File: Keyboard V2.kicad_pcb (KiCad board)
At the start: 4 copper layers, 317.8 x 142.5 mm, 239 parts, among them J1 Conn_01x05_Pin, J2 USB_C_Receptacle_USB2.0_16P, P1 SW_Push, SW1 ESC, SW10 F9, SW11 F10, SW12 F11, SW13 F12, SW14 PrntScrn, SW15 Til, SW16 1, SW17 2, SW18 3, SW19 4, SW2 F1, SW20 5, SW21 6, SW22 7, SW23 8, SW24 RotaryEncoder_Switch, SW25 9, SW26 0, SW27 Min, SW28 Plus, SW29 Bs, SW3 F2, SW30 Del, SW31 Tab, SW32 Q, SW33 W, SW34 E, SW35 R, SW36 T, SW37 Y, SW38 U, SW39 I, SW4 F3, SW40 O, SW41 P, SW42 LBrck, SW43 RBrck, SW44 BSlsh, SW45 Home, SW46 Caps, SW47 A, SW48 S, SW49 D, SW5 F4, SW50 F, SW51 G, SW52 H, SW53 J, SW54 K, SW55 L, SW56 Semi, SW57 Quot, SW58 Enter, SW59 End, SW6 F5, SW60 LShft, SW61 Z, SW62 X, SW63 C, SW64 V, SW65 B, SW66 N, SW67 M, SW68 Comma, SW69 Prd, SW7 F6, SW70 Slash, SW71 RShft, SW72 Up, SW73 LCtrl, SW74 Supr, SW75 Alt, SW76 Space, SW77 RAlt, SW78 Fn, SW79 Left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

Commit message: finish esp32-31 version
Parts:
- removed C109: 1uF, Capacitor_SMD:C_0402_1005Metric
- removed C111, C96, C97: 2.2uF, Capacitor_SMD:C_0402_1005Metric
- removed C112, C113, C114, C117, C92, C93, C94, C95: 100nF, Capacitor_SMD:C_0402_1005Metric
- removed the C78 at (339.4, 17.9)
- removed C88: 100nF, Capacitor_SMD:C_0603_1608Metric
- removed C89: 10uF, Capacitor_SMD:C_0805_2012Metric
- removed C90: 30pF, Capacitor_SMD:C_0402_1005Metric
- removed FB1: FerriteBead, Inductor_SMD:L_0603_1608Metric
- removed FID1, FID2, FID3: Fiducial, Fiducial:Fiducial_1mm_Mask2mm
- removed the R13 at (322.9, 21.0)
- removed the R16 at (321.8, 21.0)
- removed R19: 1k, Resistor_SMD:R_0603_1608Metric
- removed U2: STM32F723IEK6, STM32F723IEK6:IC_STM32F723IEK6
- removed Y1: Crystal_GND24, Crystal:Crystal_SMD_Abracon_ABM8G-4Pin_3.2x2.5mm
- added C100: 100nF, Capacitor_SMD:C_0402_1005Metric, F.Cu at (343.4, 35.5)
- added C101: 100nF, Capacitor_SMD:C_0402_1005Metric, F.Cu at (342.1, 38.7)
- added C102: 100nF, Capacitor_SMD:C_0402_1005Metric, F.Cu at (342.1, 41.8)
- added C103: 1uF, Capacitor_SMD:C_0603_1608Metric, F.Cu at (370.5, 58.6)
- added C104: 10uF, Capacitor_SMD:C_0603_1608Metric, F.Cu at (375.2, 58.1)
- added H0: MountingHole, MountingHole:MountingHole_2.2mm_M2, F.Cu at (33.4, 24.8)
- added H1: MountingHole, MountingHole:MountingHole_2.2mm_M2, F.Cu at (376.3, 149.1)
- added H10: MountingHole, MountingHole:MountingHole_2.2mm_M2, F.Cu at (183.4, 150.2)
- added H2: MountingHole, MountingHole:MountingHole_2.2mm_M2, F.Cu at (114.3, 87.9)
- added H3: MountingHole, MountingHole:MountingHole_2.2mm_M2, F.Cu at (30.5, 87.3)
- added H4: MountingHole, MountingHole:MountingHole_2.2mm_M2, F.Cu at (167.0, 24.8)
- added H5: MountingHole, MountingHole:MountingHole_2.2mm_M2, F.Cu at (30.9, 150.0)
- added H6: MountingHole, MountingHole:MountingHole_2.2mm_M2, F.Cu at (231.0, 86.4)
- added H7: MountingHole, MountingHole:MountingHole_2.2mm_M2, F.Cu at (366.6, 64.7)
- added H8: MountingHole, MountingHole:MountingHole_2.2mm_M2, F.Cu at (297.9, 24.8)
- added H9: MountingHole, MountingHole:MountingHole_2.2mm_M2, F.Cu at (377.3, 91.7)
- added J0: Fingerprint Sensor, BM06B-SRSS-TB:JST_BM06B-SRSS-TB_LF__SN_, F.Cu at (348.3, 79.7)
- added J3: Conn_01x18_Pin, FH34SRJ-18S-0.5SH(50):HRS_FH34SRJ-18S-0.5SH_50_, F.Cu at (349.5, 65.0)
- added L0: 470nH, Inductor_SMD:L_0805_2012Metric, F.Cu at (361.9, 54.6)
- added P0: SW_Push, PCM_marbastlib-various:SW_SPST_SKQG_WithStem, F.Cu at (326.0, 25.3)
- added R0: 100, Resistor_SMD:R_0402_1005Metric, F.Cu at (344.4, 83.3)
- added R10: 10K, Resistor_SMD:R_0603_1608Metric, F.Cu at (343.1, 31.9)
- added R14: 100k, Resistor_SMD:R_0402_1005Metric, F.Cu at (359.7, 52.5)
- added R17: 4.7k, Resistor_SMD:R_0402_1005Metric, F.Cu at (361.6, 46.9)
- added R4: 890, Resistor_SMD:R_0402_1005Metric, F.Cu at (372.5, 58.1)
- added R5: 10K, Resistor_SMD:R_0603_1608Metric, F.Cu at (343.1, 34.2)
- added R6: 10K, Resistor_SMD:R_0603_1608Metric, F.Cu at (341.8, 37.4)
- added R7: 10K, Resistor_SMD:R_0603_1608Metric, F.Cu at (341.8, 40.4)
- added TH0: Thermistor_NTC, Connector_JST:JST_SH_SM02B-SRSS-TB_1x02-1MP_P1.00mm_Horizontal, F.Cu at (379.1, 60.3)
- added U0: MAX17048, MAX17048G:21-0168_T822&plus_3_MXM, B.Cu at (369.9, 49.5)
- added U3: ESP32-S31-WROOM-3, ESP32-S31:ESP32-S31-WROOM-3, F.Cu at (356.6, 33.7)
- added U4: TPS62822DLC, Package_SON:Texas_VSON-HR-8_1.5x2mm_P0.5mm, F.Cu at (365.1, 53.1)
- C105, C106, C116: value 100nF -> 10uF; footprint Capacitor_SMD:C_0402_1005Metric -> Capacitor_SMD:C_0603_1608Metric
- C107, C110: value 100nF -> 100nf
- C108: value 100nF -> 4.7uF; footprint Capacitor_SMD:C_0402_1005Metric -> Capacitor_SMD:C_0603_1608Metric
- C115: value 100nF -> 1uF
- C118: value 10nF -> 10uF; footprint Capacitor_SMD:C_0402_1005Metric -> Capacitor_SMD:C_0603_1608Metric
- C120: renamed from C99; value 100pF -> 10nF; moved to B.Cu
- C121: renamed from C100; value 100pF -> 10nF; moved to B.Cu
- C122: renamed from C101; value 100pF -> 10nF; moved to B.Cu
- C123: renamed from C102; value 100pF -> 10nF; moved to B.Cu
- C124: renamed from C103; value 100pF -> 10nF; moved to B.Cu
- C125: renamed from C104; value 100pF -> 10nF; moved to B.Cu
- C91: value 30pF -> 100nF
- J1: value Conn_01x05_Pin -> Battery Connector; footprint Connector_PinHeader_2.54mm:PinHeader_1x05_P2.54mm_Horizontal -> Connector_JST:JST_PH_S2B-PH-K_1x02_P2.00mm_Horizontal; moved to F.Cu
- R1: value 100ohm -> 100; footprint Resistor_SMD:R_0603_1608Metric -> Resistor_SMD:R_0402_1005Metric
- R12: value 1k -> 10K; footprint Resistor_SMD:R_0402_1005Metric -> Resistor_SMD:R_0603_1608Metric
- R15: value 10K -> 453k
- R18: value 10K -> 4.7k; footprint Resistor_SMD:R_0603_1608Metric -> Resistor_SMD:R_0402_1005Metric
- R2: value 10K -> 100; footprint Resistor_SMD:R_0603_1608Metric -> Resistor_SMD:R_0402_1005Metric
- R20: renamed from R6; value 100R -> 100; moved to B.Cu
- R21: renamed from R7; value 100R -> 100; moved to B.Cu
- R22: renamed from R8; value 100R -> 100; moved to B.Cu
- R23: renamed from R9; value 100R -> 100; moved to B.Cu
- R24: renamed from R10; value 100R -> 100; moved to B.Cu
- R25: renamed from R11; value 100R -> 100; moved to B.Cu
- R3: value 3.00K -> 1.5k; footprint Resistor_SMD:R_0603_1608Metric -> Resistor_SMD:R_0402_1005Metric
- R8: renamed from R17; value 22R -> 22
- R9: renamed from R14; value 22R -> 22
- SW0: renamed from SW1; footprint PCM_marbastlib-he:SW_MX_HE_0deg_1u_DFN -> A1395SEHLT-T:SENSOR_A1395SEHLT-T; moved to B.Cu
- SW1: renamed from SW2; footprint PCM_marbastlib-he:SW_MX_HE_0deg_1u_DFN -> A1395SEHLT-T:SENSOR_A1395SEHLT-T; moved to B.Cu
- SW10: renamed from SW11; footprint PCM_marbastlib-he:SW_MX_HE_0deg_1u_DFN -> A1395SEHLT-T:SENSOR_A1395SEHLT-T; moved to B.Cu
- SW11: renamed from SW12; footprint PCM_marbastlib-he:SW_MX_HE_0deg_1u_DFN -> A1395SEHLT-T:SENSOR_A1395SEHLT-T; moved to B.Cu
- SW12: renamed from SW13; footprint PCM_marbastlib-he:SW_MX_HE_0deg_1u_DFN -> A1395SEHLT-T:SENSOR_A1395SEHLT-T; moved to B.Cu
- SW13: renamed from SW14; footprint PCM_marbastlib-he:SW_MX_HE_0deg_1u_DFN -> A1395SEHLT-T:SENSOR_A1395SEHLT-T; moved to B.Cu
- SW14: renamed from SW15; footprint PCM_marbastlib-he:SW_MX_HE_0deg_1u_DFN -> A1395SEHLT-T:SENSOR_A1395SEHLT-T; moved to B.Cu
- SW15: renamed from SW16; footprint PCM_marbastlib-he:SW_MX_HE_0deg_1u_DFN -> A1395SEHLT-T:SENSOR_A1395SEHLT-T; moved to B.Cu
- SW16: renamed from SW17; footprint PCM_marbastlib-he:SW_MX_HE_0deg_1u_DFN -> A1395SEHLT-T:SENSOR_A1395SEHLT-T; moved to B.Cu
- SW17: renamed from SW18; footprint PCM_marbastlib-he:SW_MX_HE_0deg_1u_DFN -> A1395SEHLT-T:SENSOR_A1395SEHLT-T; moved to B.Cu
- SW18: renamed from SW19; footprint PCM_marbastlib-he:SW_MX_HE_0deg_1u_DFN -> A1395SEHLT-T:SENSOR_A1395SEHLT-T; moved to B.Cu
- SW19: renamed from SW20; footprint PCM_marbastlib-he:SW_MX_HE_0deg_1u_DFN -> A1395SEHLT-T:SENSOR_A1395SEHLT-T; moved to B.Cu
- SW2: renamed from SW3; footprint PCM_marbastlib-he:SW_MX_HE_0deg_1u_DFN -> A1395SEHLT-T:SENSOR_A1395SEHLT-T; moved to B.Cu
- SW20: renamed from SW21; footprint PCM_marbastlib-he:SW_MX_HE_0deg_1u_DFN -> A1395SEHLT-T:SENSOR_A1395SEHLT-T; moved to B.Cu
- SW21: renamed from SW22; footprint PCM_marbastlib-he:SW_MX_HE_0deg_1u_DFN -> A1395SEHLT-T:SENSOR_A1395SEHLT-T; moved to B.Cu
- SW22: renamed from SW23; footprint PCM_marbastlib-he:SW_MX_HE_0deg_1u_DFN -> A1395SEHLT-T:SENSOR_A1395SEHLT-T; moved to B.Cu
- SW24: renamed from SW25; footprint PCM_marbastlib-he:SW_MX_HE_0deg_1u_DFN -> A1395SEHLT-T:SENSOR_A1395SEHLT-T; moved to B.Cu
- SW25: renamed from SW26; footprint PCM_marbastlib-he:SW_MX_HE_0deg_1u_DFN -> A1395SEHLT-T:SENSOR_A1395SEHLT-T; moved to B.Cu
- SW26: renamed from SW27; footprint PCM_marbastlib-he:SW_MX_HE_0deg_1u_DFN -> A1395SEHLT-T:SENSOR_A1395SEHLT-T; moved to B.Cu
- SW27: renamed from SW28; footprint PCM_marbastlib-he:SW_MX_HE_0deg_1u_DFN -> A1395SEHLT-T:SENSOR_A1395SEHLT-T; moved to B.Cu
- SW28: renamed from SW29; footprint PCM_marbastlib-he:SW_MX_HE_0deg_1u_DFN -> A1395SEHLT-T:SENSOR_A1395SEHLT-T; moved to B.Cu
- SW29: renamed from SW30; footprint PCM_marbastlib-he:SW_MX_HE_0deg_1u_DFN -> A1395SEHLT-T:SENSOR_A1395SEHLT-T; moved to B.Cu
- SW3: renamed from SW4; footprint PCM_marbastlib-he:SW_MX_HE_0deg_1u_DFN -> A1395SEHLT-T:SENSOR_A1395SEHLT-T; moved to B.Cu
- SW30: renamed from SW31; footprint PCM_marbastlib-he:SW_MX_HE_0deg_1u_DFN -> A1395SEHLT-T:SENSOR_A1395SEHLT-T; moved to B.Cu
- SW31: renamed from SW32; footprint PCM_marbastlib-he:SW_MX_HE_0deg_1u_DFN -> A1395SEHLT-T:SENSOR_A1395SEHLT-T; moved to B.Cu
- SW32: renamed from SW33; footprint PCM_marbastlib-he:SW_MX_HE_0deg_1u_DFN -> A1395SEHLT-T:SENSOR_A1395SEHLT-T; moved to B.Cu
- SW33: renamed from SW34; footprint PCM_marbastlib-he:SW_MX_HE_0deg_1u_DFN -> A1395SEHLT-T:SENSOR_A1395SEHLT-T; moved to B.Cu
- SW34: renamed from SW35; footprint PCM_marbastlib-he:SW_MX_HE_0deg_1u_DFN -> A1395SEHLT-T:SENSOR_A1395SEHLT-T; moved to B.Cu
- SW35: renamed from SW36; footprint PCM_marbastlib-he:SW_MX_HE_0deg_1u_DFN -> A1395SEHLT-T:SENSOR_A1395SEHLT-T; moved to B.Cu
- SW36: renamed from SW37; footprint PCM_marbastlib-he:SW_MX_HE_0deg_1u_DFN -> A1395SEHLT-T:SENSOR_A1395SEHLT-T; moved to B.Cu
- SW37: renamed from SW38; footprint PCM_marbastlib-he:SW_MX_HE_0deg_1u_DFN -> A1395SEHLT-T:SENSOR_A1395SEHLT-T; moved to B.Cu
- SW38: renamed from SW39; footprint PCM_marbastlib-he:SW_MX_HE_0deg_1u_DFN -> A1395SEHLT-T:SENSOR_A1395SEHLT-T; moved to B.Cu
- SW39: renamed from SW40; footprint PCM_marbastlib-he:SW_MX_HE_0deg_1u_DFN -> A1395SEHLT-T:SENSOR_A1395SEHLT-T; moved to B.Cu
- SW4: renamed from SW5; footprint PCM_marbastlib-he:SW_MX_HE_0deg_1u_DFN -> A1395SEHLT-T:SENSOR_A1395SEHLT-T; moved to B.Cu
- SW40: renamed from SW41; footprint PCM_marbastlib-he:SW_MX_HE_0deg_1u_DFN -> A1395SEHLT-T:SENSOR_A1395SEHLT-T; moved to B.Cu
- SW41: renamed from SW42; footprint PCM_marbastlib-he:SW_MX_HE_0deg_1u_DFN -> A1395SEHLT-T:SENSOR_A1395SEHLT-T; moved to B.Cu
- SW42: renamed from SW43; footprint PCM_marbastlib-he:SW_MX_HE_0deg_1u_DFN -> A1395SEHLT-T:SENSOR_A1395SEHLT-T; moved to B.Cu
- SW43: renamed from SW44; footprint PCM_marbastlib-he:SW_MX_HE_0deg_1u_DFN -> A1395SEHLT-T:SENSOR_A1395SEHLT-T; moved to B.Cu
- SW44: renamed from SW45; footprint PCM_marbastlib-he:SW_MX_HE_0deg_1u_DFN -> A1395SEHLT-T:SENSOR_A1395SEHLT-T; moved to B.Cu
- SW45: renamed from SW46; footprint PCM_marbastlib-he:SW_MX_HE_0deg_1u_DFN -> A1395SEHLT-T:SENSOR_A1395SEHLT-T; moved to B.Cu
- SW46: renamed from SW47; footprint PCM_marbastlib-he:SW_MX_HE_0deg_1u_DFN -> A1395SEHLT-T:SENSOR_A1395SEHLT-T; moved to B.Cu
- SW47: renamed from SW48; footprint PCM_marbastlib-he:SW_MX_HE_0deg_1u_DFN -> A1395SEHLT-T:SENSOR_A1395SEHLT-T; moved to B.Cu
- SW48: renamed from SW49; footprint PCM_marbastlib-he:SW_MX_HE_0deg_1u_DFN -> A1395SEHLT-T:SENSOR_A1395SEHLT-T; moved to B.Cu
- SW49: renamed from SW50; footprint PCM_marbastlib-he:SW_MX_HE_0deg_1u_DFN -> A1395SEHLT-T:SENSOR_A1395SEHLT-T; moved to B.Cu
- SW5: renamed from SW6; footprint PCM_marbastlib-he:SW_MX_HE_0deg_1u_DFN -> A1395SEHLT-T:SENSOR_A1395SEHLT-T; moved to B.Cu
- SW50: renamed from SW51; footprint PCM_marbastlib-he:SW_MX_HE_0deg_1u_DFN -> A1395SEHLT-T:SENSOR_A1395SEHLT-T; moved to B.Cu
- SW51: renamed from SW52; footprint PCM_marbastlib-he:SW_MX_HE_0deg_1u_DFN -> A1395SEHLT-T:SENSOR_A1395SEHLT-T; moved to B.Cu
- SW52: renamed from SW53; footprint PCM_marbastlib-he:SW_MX_HE_0deg_1u_DFN -> A1395SEHLT-T:SENSOR_A1395SEHLT-T; moved to B.Cu
- SW53: renamed from SW54; footprint PCM_marbastlib-he:SW_MX_HE_0deg_1u_DFN -> A1395SEHLT-T:SENSOR_A1395SEHLT-T; moved to B.Cu
- SW54: renamed from SW55; footprint PCM_marbastlib-he:SW_MX_HE_0deg_1u_DFN -> A1395SEHLT-T:SENSOR_A1395SEHLT-T; moved to B.Cu
- SW55: renamed from SW56; footprint PCM_marbastlib-he:SW_MX_HE_0deg_1u_DFN -> A1395SEHLT-T:SENSOR_A1395SEHLT-T; moved to B.Cu
- SW56: renamed from SW57; footprint PCM_marbastlib-he:SW_MX_HE_0deg_1u_DFN -> A1395SEHLT-T:SENSOR_A1395SEHLT-T; moved to B.Cu
- SW57: renamed from SW58; footprint PCM_marbastlib-he:SW_MX_HE_0deg_1u_DFN -> A1395SEHLT-T:SENSOR_A1395SEHLT-T; moved to B.Cu
- SW58: renamed from SW59; footprint PCM_marbastlib-he:SW_MX_HE_0deg_1u_DFN -> A1395SEHLT-T:SENSOR_A1395SEHLT-T; moved to B.Cu
- SW59: renamed from SW60; footprint PCM_marbastlib-he:SW_MX_HE_0deg_1u_DFN -> A1395SEHLT-T:SENSOR_A1395SEHLT-T; moved to B.Cu
- SW6: renamed from SW7; footprint PCM_marbastlib-he:SW_MX_HE_0deg_1u_DFN -> A1395SEHLT-T:SENSOR_A1395SEHLT-T; moved to B.Cu
- SW60: renamed from SW61; footprint PCM_marbastlib-he:SW_MX_HE_0deg_1u_DFN -> A1395SEHLT-T:SENSOR_A1395SEHLT-T; moved to B.Cu
- SW61: renamed from SW62; footprint PCM_marbastlib-he:SW_MX_HE_0deg_1u_DFN -> A1395SEHLT-T:SENSOR_A1395SEHLT-T; moved to B.Cu
- SW62: renamed from SW63; footprint PCM_marbastlib-he:SW_MX_HE_0deg_1u_DFN -> A1395SEHLT-T:SENSOR_A1395SEHLT-T; moved to B.Cu
- SW63: renamed from SW64; footprint PCM_marbastlib-he:SW_MX_HE_0deg_1u_DFN -> A1395SEHLT-T:SENSOR_A1395SEHLT-T; moved to B.Cu
- SW64: renamed from SW65; footprint PCM_marbastlib-he:SW_MX_HE_0deg_1u_DFN -> A1395SEHLT-T:SENSOR_A1395SEHLT-T; moved to B.Cu
- SW65: renamed from SW66; footprint PCM_marbastlib-he:SW_MX_HE_0deg_1u_DFN -> A1395SEHLT-T:SENSOR_A1395SEHLT-T; moved to B.Cu
- SW66: renamed from SW67; footprint PCM_marbastlib-he:SW_MX_HE_0deg_1u_DFN -> A1395SEHLT-T:SENSOR_A1395SEHLT-T; moved to B.Cu
- SW67: renamed from SW68; footprint PCM_marbastlib-he:SW_MX_HE_0deg_1u_DFN -> A1395SEHLT-T:SENSOR_A1395SEHLT-T; moved to B.Cu
- SW68: renamed from SW69; footprint PCM_marbastlib-he:SW_MX_HE_0deg_1u_DFN -> A1395SEHLT-T:SENSOR_A1395SEHLT-T; moved to B.Cu
- SW69: renamed from SW70; footprint PCM_marbastlib-he:SW_MX_HE_0deg_1u_DFN -> A1395SEHLT-T:SENSOR_A1395SEHLT-T; moved to B.Cu
- SW7: renamed from SW8; footprint PCM_marbastlib-he:SW_MX_HE_0deg_1u_DFN -> A1395SEHLT-T:SENSOR_A1395SEHLT-T; moved to B.Cu
- SW70: renamed from SW71; footprint PCM_marbastlib-he:SW_MX_HE_0deg_1u_DFN -> A1395SEHLT-T:SENSOR_A1395SEHLT-T; moved to B.Cu
- SW71: renamed from SW72; footprint PCM_marbastlib-he:SW_MX_HE_0deg_1u_DFN -> A1395SEHLT-T:SENSOR_A1395SEHLT-T; moved to B.Cu
- SW72: renamed from SW73; footprint PCM_marbastlib-he:SW_MX_HE_0deg_1u_DFN -> A1395SEHLT-T:SENSOR_A1395SEHLT-T; moved to B.Cu
- SW73: renamed from SW74; footprint PCM_marbastlib-he:SW_MX_HE_0deg_1u_DFN -> A1395SEHLT-T:SENSOR_A1395SEHLT-T; moved to B.Cu
- SW74: renamed from SW75; footprint PCM_marbastlib-he:SW_MX_HE_0deg_1u_DFN -> A1395SEHLT-T:SENSOR_A1395SEHLT-T; moved to B.Cu
- SW75: renamed from SW76; footprint PCM_marbastlib-he:SW_MX_HE_0deg_1u_DFN -> A1395SEHLT-T:SENSOR_A1395SEHLT-T; moved to B.Cu
- SW76: renamed from SW77; footprint PCM_marbastlib-he:SW_MX_HE_0deg_1u_DFN -> A1395SEHLT-T:SENSOR_A1395SEHLT-T; moved to B.Cu
- SW77: renamed from SW78; footprint PCM_marbastlib-he:SW_MX_HE_0deg_1u_DFN -> A1395SEHLT-T:SENSOR_A1395SEHLT-T; moved to B.Cu
- SW78: renamed from SW79; footprint PCM_marbastlib-he:SW_MX_HE_0deg_1u_DFN -> A1395SEHLT-T:SENSOR_A1395SEHLT-T; moved to B.Cu
- SW79: renamed from SW80; footprint PCM_marbastlib-he:SW_MX_HE_0deg_1u_DFN -> A1395SEHLT-T:SENSOR_A1395SEHLT-T; moved to B.Cu
- SW8: renamed from SW9; footprint PCM_marbastlib-he:SW_MX_HE_0deg_1u_DFN -> A1395SEHLT-T:SENSOR_A1395SEHLT-T; moved to B.Cu
- SW80: renamed from SW81; footprint PCM_marbastlib-he:SW_MX_HE_0deg_1u_DFN -> A1395SEHLT-T:SENSOR_A1395SEHLT-T; moved to B.Cu
- SW9: renamed from SW10; footprint PCM_marbastlib-he:SW_MX_HE_0deg_1u_DFN -> A1395SEHLT-T:SENSOR_A1395SEHLT-T; moved to B.Cu
- U1: value MCP1700T-3302E/MAY -> BQ24075RGT; footprint footprints:DFN-S6_2x2MC_MCH -> Package_DFN_QFN:VQFN-16-1EP_3x3mm_P0.5mm_EP1.6x1.6mm
- moved R2 75.0 mm to (344.5, 80.2), turned to 180 degrees
- moved C91 73.6 mm to (344.5, 82.2), turned to 180 degrees
- moved C105 70.8 mm to (368.7, 53.0), turned to -90 degrees
- moved R1 70.1 mm to (344.5, 79.1)
- moved C98 67.1 mm to (346.4, 74.5)
- moved R3 57.8 mm to (368.9, 56.6), turned to -90 degrees
- moved C108 53.5 mm to (367.1, 53.0), turned to -90 degrees
- moved C116 51.1 mm to (357.8, 55.4), turned to 90 degrees
- moved R9 50.3 mm to (360.4, 46.9), turned to 90 degrees
- moved R15 48.9 mm to (360.8, 52.5), turned to 90 degrees
- moved R8 48.9 mm to (359.4, 46.9), turned to 90 degrees
- moved C118 47.5 mm to (359.3, 55.4), turned to 90 degrees
- moved C120 47.1 mm to (343.9, 53.7), turned to 180 degrees
- moved U1 47.1 mm to (371.6, 54.9), turned to 180 degrees
- moved R18 46.9 mm to (362.7, 46.9), turned to 90 degrees
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- renumbered C1 to C0, C2 to C1, C11 to C10, C12 to C11, C13 to C12, C14 to C13, C15 to C14, C16 to C15, C17 to C16, C18 to C17, C19 to C18, C20 to C19, C3 to C2, C21 to C20, C22 to C21, C23 to C22, C24 to C23, C25 to C24, C26 to C25, C27 to C26, C28 to C27, C29 to C28, C30 to C29, C4 to C3, C31 to C30, C32 to C31, C33 to C32, C34 to C33, C35 to C34, C36 to C35, C37 to C36, C38 to C37, C39 to C38, C40 to C39, C5 to C4, C41 to C40, C42 to C41, C43 to C42, C44 to C43, C45 to C44, C46 to C45, C47 to C46, C48 to C47, C49 to C48, C50 to C49, C6 to C5, C51 to C50, C52 to C51, C53 to C52, C54 to C53, C55 to C54, C56 to C55, C57 to C56, C58 to C57, C59 to C58, C60 to C59, C7 to C6, C61 to C60, C62 to C61, C63 to C62, C64 to C63, C65 to C64, C66 to C65, C67 to C66, C68 to C67, C69 to C68, C70 to C69, C8 to C7, C71 to C70, C72 to C71, C73 to C72, C74 to C73, C75 to C74, C76 to C75, C77 to C76, C79 to C77, C80 to C78, C81 to C79, C9 to C8, C82 to C80, C83 to C81, C84 to C82, C85 to C83, C86 to C84, C87 to C85, C10 to C9, R4 to R13, R5 to R16, S1 to S0, S2 to S1, S3 to S2, S4 to S3, SW24 to SW23, U3 to U5
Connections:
- AM0 pad 24: +3V3A -> +3V3
- AM1 pad 24: +3V3A -> +3V3
- AM2 pad 24: +3V3A -> +3V3
- AM3 pad 24: +3V3A -> +3V3
- AM4 pad 24: +3V3A -> +3V3
- AM5 pad 24: +3V3A -> +3V3
- C0 pad 2: +3V3A -> +3V3
- C1 pad 2: +3V3A -> +3V3
- C10 pad 2: +3V3A -> +3V3
- C105 pad 2: +3V3 -> Net-(U4-EN)
- C106 pad 1: +3V3 -> GND
- C106 pad 2: GND -> +3V3
- C107 pad 1: +3V3 -> GND
- C107 pad 2: GND -> +3V3
- C108 pad 1: +3V3 -> GND
- C108 pad 2: GND -> Net-(U4-EN)
- C11 pad 2: +3V3A -> +3V3
- C110 pad 1: +3V3 -> GND
- C110 pad 2: GND -> +3V3
- C115 pad 1: GND -> Net-(U3-EN)
- C115 pad 2: +3V3A -> GND
- C118 pad 1: Net-(U2B-PD11) -> GND
- C118 pad 2: GND -> +3V3
- C12 pad 2: +3V3A -> +3V3
- C13 pad 2: +3V3A -> +3V3
- C14 pad 2: +3V3A -> +3V3
- C15 pad 2: +3V3A -> +3V3
- C16 pad 2: +3V3A -> +3V3
- C17 pad 2: +3V3A -> +3V3
- C18 pad 2: +3V3A -> +3V3
- C19 pad 2: +3V3A -> +3V3
- C2 pad 2: +3V3A -> +3V3
- C20 pad 2: +3V3A -> +3V3
- C21 pad 2: +3V3A -> +3V3
- C22 pad 2: +3V3A -> +3V3
- C23 pad 2: +3V3A -> +3V3
- C24 pad 2: +3V3A -> +3V3
- C25 pad 2: +3V3A -> +3V3
- C26 pad 2: +3V3A -> +3V3
- C27 pad 2: +3V3A -> +3V3
- C28 pad 2: +3V3A -> +3V3
- C29 pad 2: +3V3A -> +3V3
- C3 pad 2: +3V3A -> +3V3
- C30 pad 2: +3V3A -> +3V3
- C31 pad 2: +3V3A -> +3V3
- C32 pad 2: +3V3A -> +3V3
- C33 pad 2: +3V3A -> +3V3
- C34 pad 2: +3V3A -> +3V3
- C35 pad 2: +3V3A -> +3V3
- C36 pad 2: +3V3A -> +3V3
- C37 pad 2: +3V3A -> +3V3
- C38 pad 2: +3V3A -> +3V3
- C39 pad 2: +3V3A -> +3V3
- C4 pad 2: +3V3A -> +3V3
- C40 pad 2: +3V3A -> +3V3
- C41 pad 2: +3V3A -> +3V3
- C42 pad 2: +3V3A -> +3V3
- C43 pad 2: +3V3A -> +3V3
- C44 pad 2: +3V3A -> +3V3
- C45 pad 2: +3V3A -> +3V3
- C46 pad 2: +3V3A -> +3V3
- C47 pad 2: +3V3A -> +3V3
- C48 pad 2: +3V3A -> +3V3
- C49 pad 2: +3V3A -> +3V3
- C5 pad 2: +3V3A -> +3V3
- C50 pad 2: +3V3A -> +3V3
- C51 pad 2: +3V3A -> +3V3
- C52 pad 2: +3V3A -> +3V3
- C53 pad 2: +3V3A -> +3V3
- C54 pad 2: +3V3A -> +3V3
- C55 pad 2: +3V3A -> +3V3
- C56 pad 2: +3V3A -> +3V3
- C57 pad 2: +3V3A -> +3V3
- C58 pad 2: +3V3A -> +3V3
- C59 pad 2: +3V3A -> +3V3
- C6 pad 2: +3V3A -> +3V3
- C60 pad 2: +3V3A -> +3V3
- C61 pad 2: +3V3A -> +3V3
- C62 pad 2: +3V3A -> +3V3
- C63 pad 2: +3V3A -> +3V3
- C64 pad 2: +3V3A -> +3V3
- C65 pad 2: +3V3A -> +3V3
- C66 pad 2: +3V3A -> +3V3
- C67 pad 2: +3V3A -> +3V3
- C68 pad 2: +3V3A -> +3V3
- C69 pad 2: +3V3A -> +3V3
- C7 pad 2: +3V3A -> +3V3
- C70 pad 2: +3V3A -> +3V3
- C71 pad 2: +3V3A -> +3V3
- C72 pad 2: +3V3A -> +3V3
- C73 pad 2: +3V3A -> +3V3
- C74 pad 2: +3V3A -> +3V3
- C75 pad 2: +3V3A -> +3V3
- C76 pad 2: +3V3A -> +3V3
- C77 pad 2: +3V3A -> +3V3
- C78 pad 2: +3V3A -> +3V3
- C79 pad 2: +3V3A -> +3V3
- C8 pad 2: +3V3A -> +3V3
- C80 pad 2: +3V3A -> +3V3
- C81 pad 2: +3V3A -> +3V3
- C82 pad 2: +3V3A -> +3V3
- C83 pad 2: +3V3A -> +3V3
- C84 pad 2: +3V3A -> +3V3
- C85 pad 2: +3V3A -> +3V3
- C9 pad 2: +3V3A -> +3V3
- C91 pad 1: Net-(C91-Pad1) -> Net-(J0-Pin_6)
- C98 pad 1: GND -> +3V3
- C98 pad 2: +3V3 -> GND
- J1 pad 1: +3V3 -> BAT+
- J1 pad 2: SWDIO -> GND
- P1 pad 1: GND -> Net-(U3-EN)
- P1 pad 2: Net-(U2C-~{RST}) -> GND
- R1 pad 2: Net-(C91-Pad1) -> TXD_FPRINT
- R12 pad 1: Net-(U2B-PC6) -> Net-(U3-EN)
- R12 pad 2: ENC_A -> +3V3
- R15 pad 1: Net-(U2B-PC6) -> +3V3
- R15 pad 2: +3V3 -> Net-(U4-FB)
- R18 pad 1: Net-(U2B-PD11) -> CARGE_SDA
- R18 pad 2: +3V3 -> Net-(U3-IO34)
- R2 pad 1: GND -> Net-(J0-Pin_4)
- R2 pad 2: Net-(U2C-BOOT0) -> RXD_FPRINT
- R20 pad 1: MUX_0 -> MUX_5
- R21 pad 1: MUX_1 -> MUX_4
- R22 pad 1: MUX_4 -> MUX_3
- R24 pad 1: MUX_3 -> MUX_1
- R25 pad 1: MUX_5 -> MUX_0
- R3 pad 1: GND -> Net-(U1-ILIM)
- R3 pad 2: Net-(U2C-OTG_HS_REXT) -> GND
- SW0 pad 1: +3V3A -> +3V3
- SW0 pad 5: +3V3A -> HALL_PWR_ON
- SW0 pad 6: +3V3A -> +3V3
- SW1 pad 1: +3V3A -> +3V3
- SW1 pad 5: +3V3A -> HALL_PWR_ON
- SW1 pad 6: +3V3A -> +3V3
- SW10 pad 1: +3V3A -> +3V3
- SW10 pad 5: +3V3A -> HALL_PWR_ON
- SW10 pad 6: +3V3A -> +3V3
- SW11 pad 1: +3V3A -> +3V3
- SW11 pad 5: +3V3A -> HALL_PWR_ON
- SW11 pad 6: +3V3A -> +3V3
- SW12 pad 1: +3V3A -> +3V3
- SW12 pad 5: +3V3A -> HALL_PWR_ON
- SW12 pad 6: +3V3A -> +3V3
- SW13 pad 1: +3V3A -> +3V3
- SW13 pad 5: +3V3A -> HALL_PWR_ON
- SW13 pad 6: +3V3A -> +3V3
- SW14 pad 1: +3V3A -> +3V3
- SW14 pad 5: +3V3A -> HALL_PWR_ON
- SW14 pad 6: +3V3A -> +3V3
- SW15 pad 1: +3V3A -> +3V3
- SW15 pad 5: +3V3A -> HALL_PWR_ON
- SW15 pad 6: +3V3A -> +3V3
- SW16 pad 1: +3V3A -> +3V3
- SW16 pad 5: +3V3A -> HALL_PWR_ON
- SW16 pad 6: +3V3A -> +3V3
- SW17 pad 1: +3V3A -> +3V3
- SW17 pad 5: +3V3A -> HALL_PWR_ON
- SW17 pad 6: +3V3A -> +3V3
- SW18 pad 1: +3V3A -> +3V3
- SW18 pad 5: +3V3A -> HALL_PWR_ON
- SW18 pad 6: +3V3A -> +3V3
- SW19 pad 1: +3V3A -> +3V3
- SW19 pad 5: +3V3A -> HALL_PWR_ON
- SW19 pad 6: +3V3A -> +3V3
- SW2 pad 1: +3V3A -> +3V3
- SW2 pad 5: +3V3A -> HALL_PWR_ON
- SW2 pad 6: +3V3A -> +3V3
- SW20 pad 1: +3V3A -> +3V3
- SW20 pad 5: +3V3A -> HALL_PWR_ON
- SW20 pad 6: +3V3A -> +3V3
- SW21 pad 1: +3V3A -> +3V3
- SW21 pad 5: +3V3A -> HALL_PWR_ON
- SW21 pad 6: +3V3A -> +3V3
- SW22 pad 1: +3V3A -> +3V3
- SW22 pad 5: +3V3A -> HALL_PWR_ON
- SW22 pad 6: +3V3A -> +3V3
- SW24 pad 1: +3V3A -> +3V3
- SW24 pad 5: +3V3A -> HALL_PWR_ON
- SW24 pad 6: +3V3A -> +3V3
- SW25 pad 1: +3V3A -> +3V3
- SW25 pad 5: +3V3A -> HALL_PWR_ON
- SW25 pad 6: +3V3A -> +3V3
- SW26 pad 1: +3V3A -> +3V3
- SW26 pad 5: +3V3A -> HALL_PWR_ON
- SW26 pad 6: +3V3A -> +3V3
- SW27 pad 1: +3V3A -> +3V3
- SW27 pad 5: +3V3A -> HALL_PWR_ON
- SW27 pad 6: +3V3A -> +3V3
- SW28 pad 1: +3V3A -> +3V3
- SW28 pad 5: +3V3A -> HALL_PWR_ON
- SW28 pad 6: +3V3A -> +3V3
- SW29 pad 1: +3V3A -> +3V3
- SW29 pad 5: +3V3A -> HALL_PWR_ON
- SW29 pad 6: +3V3A -> +3V3
- SW3 pad 1: +3V3A -> +3V3
- SW3 pad 5: +3V3A -> HALL_PWR_ON
- SW3 pad 6: +3V3A -> +3V3
- SW30 pad 1: +3V3A -> +3V3
- SW30 pad 5: +3V3A -> HALL_PWR_ON
- SW30 pad 6: +3V3A -> +3V3
- SW31 pad 1: +3V3A -> +3V3
- SW31 pad 5: +3V3A -> HALL_PWR_ON
- SW31 pad 6: +3V3A -> +3V3
- SW32 pad 1: +3V3A -> +3V3
- SW32 pad 5: +3V3A -> HALL_PWR_ON
- SW32 pad 6: +3V3A -> +3V3
- SW33 pad 1: +3V3A -> +3V3
- SW33 pad 5: +3V3A -> HALL_PWR_ON
- SW33 pad 6: +3V3A -> +3V3
- SW34 pad 1: +3V3A -> +3V3
- SW34 pad 5: +3V3A -> HALL_PWR_ON
- SW34 pad 6: +3V3A -> +3V3
- SW35 pad 1: +3V3A -> +3V3
- SW35 pad 5: +3V3A -> HALL_PWR_ON
- SW35 pad 6: +3V3A -> +3V3
- SW36 pad 1: +3V3A -> +3V3
- SW36 pad 5: +3V3A -> HALL_PWR_ON
- SW36 pad 6: +3V3A -> +3V3
- SW37 pad 1: +3V3A -> +3V3
- SW37 pad 5: +3V3A -> HALL_PWR_ON
- SW37 pad 6: +3V3A -> +3V3
- SW38 pad 1: +3V3A -> +3V3
- SW38 pad 5: +3V3A -> HALL_PWR_ON
- SW38 pad 6: +3V3A -> +3V3
- SW39 pad 1: +3V3A -> +3V3
- SW39 pad 5: +3V3A -> HALL_PWR_ON
- SW39 pad 6: +3V3A -> +3V3
- SW4 pad 1: +3V3A -> +3V3
- SW4 pad 5: +3V3A -> HALL_PWR_ON
- SW4 pad 6: +3V3A -> +3V3
- SW40 pad 1: +3V3A -> +3V3
- SW40 pad 5: +3V3A -> HALL_PWR_ON
- SW40 pad 6: +3V3A -> +3V3
- SW41 pad 1: +3V3A -> +3V3
- SW41 pad 5: +3V3A -> HALL_PWR_ON
- SW41 pad 6: +3V3A -> +3V3
- SW42 pad 1: +3V3A -> +3V3
- SW42 pad 5: +3V3A -> HALL_PWR_ON
- SW42 pad 6: +3V3A -> +3V3
- SW43 pad 1: +3V3A -> +3V3
- SW43 pad 5: +3V3A -> HALL_PWR_ON
- SW43 pad 6: +3V3A -> +3V3
- SW44 pad 1: +3V3A -> +3V3
- SW44 pad 5: +3V3A -> HALL_PWR_ON
- SW44 pad 6: +3V3A -> +3V3
- SW45 pad 1: +3V3A -> +3V3
- SW45 pad 5: +3V3A -> HALL_PWR_ON
- SW45 pad 6: +3V3A -> +3V3
- SW46 pad 1: +3V3A -> +3V3
- SW46 pad 5: +3V3A -> HALL_PWR_ON
- SW46 pad 6: +3V3A -> +3V3
- SW47 pad 1: +3V3A -> +3V3
- SW47 pad 5: +3V3A -> HALL_PWR_ON
- SW47 pad 6: +3V3A -> +3V3
- SW48 pad 1: +3V3A -> +3V3
- SW48 pad 5: +3V3A -> HALL_PWR_ON
- SW48 pad 6: +3V3A -> +3V3
- SW49 pad 1: +3V3A -> +3V3
- SW49 pad 5: +3V3A -> HALL_PWR_ON
- SW49 pad 6: +3V3A -> +3V3
- SW5 pad 1: +3V3A -> +3V3
- SW5 pad 5: +3V3A -> HALL_PWR_ON
- SW5 pad 6: +3V3A -> +3V3
- SW50 pad 1: +3V3A -> +3V3
- SW50 pad 5: +3V3A -> HALL_PWR_ON
- SW50 pad 6: +3V3A -> +3V3
- SW51 pad 1: +3V3A -> +3V3
- SW51 pad 5: +3V3A -> HALL_PWR_ON
- SW51 pad 6: +3V3A -> +3V3
- SW52 pad 1: +3V3A -> +3V3
- SW52 pad 5: +3V3A -> HALL_PWR_ON
- SW52 pad 6: +3V3A -> +3V3
- SW53 pad 1: +3V3A -> +3V3
- SW53 pad 5: +3V3A -> HALL_PWR_ON
- SW53 pad 6: +3V3A -> +3V3
- SW54 pad 1: +3V3A -> +3V3
- SW54 pad 5: +3V3A -> HALL_PWR_ON
- SW54 pad 6: +3V3A -> +3V3
- SW55 pad 1: +3V3A -> +3V3
- SW55 pad 5: +3V3A -> HALL_PWR_ON
- SW55 pad 6: +3V3A -> +3V3
- SW56 pad 1: +3V3A -> +3V3
- SW56 pad 5: +3V3A -> HALL_PWR_ON
- SW56 pad 6: +3V3A -> +3V3
- SW57 pad 1: +3V3A -> +3V3
- SW57 pad 5: +3V3A -> HALL_PWR_ON
- SW57 pad 6: +3V3A -> +3V3
- SW58 pad 1: +3V3A -> +3V3
- SW58 pad 5: +3V3A -> HALL_PWR_ON
- SW58 pad 6: +3V3A -> +3V3
- SW59 pad 1: +3V3A -> +3V3
- SW59 pad 5: +3V3A -> HALL_PWR_ON
- SW59 pad 6: +3V3A -> +3V3
- SW6 pad 1: +3V3A -> +3V3
- SW6 pad 5: +3V3A -> HALL_PWR_ON
- SW6 pad 6: +3V3A -> +3V3
- SW60 pad 1: +3V3A -> +3V3
- SW60 pad 5: +3V3A -> HALL_PWR_ON
- SW60 pad 6: +3V3A -> +3V3
- SW61 pad 1: +3V3A -> +3V3
- SW61 pad 5: +3V3A -> HALL_PWR_ON
- SW61 pad 6: +3V3A -> +3V3
- SW62 pad 1: +3V3A -> +3V3
- SW62 pad 5: +3V3A -> HALL_PWR_ON
- SW62 pad 6: +3V3A -> +3V3
- SW63 pad 1: +3V3A -> +3V3
- SW63 pad 5: +3V3A -> HALL_PWR_ON
- SW63 pad 6: +3V3A -> +3V3
- SW64 pad 1: +3V3A -> +3V3
- SW64 pad 5: +3V3A -> HALL_PWR_ON
- SW64 pad 6: +3V3A -> +3V3
- SW65 pad 1: +3V3A -> +3V3
- SW65 pad 5: +3V3A -> HALL_PWR_ON
- SW65 pad 6: +3V3A -> +3V3
- SW66 pad 1: +3V3A -> +3V3
- SW66 pad 5: +3V3A -> HALL_PWR_ON
- SW66 pad 6: +3V3A -> +3V3
- SW67 pad 1: +3V3A -> +3V3
- SW67 pad 5: +3V3A -> HALL_PWR_ON
- SW67 pad 6: +3V3A -> +3V3
- SW68 pad 1: +3V3A -> +3V3
- SW68 pad 5: +3V3A -> HALL_PWR_ON
- SW68 pad 6: +3V3A -> +3V3
- SW69 pad 1: +3V3A -> +3V3
- SW69 pad 5: +3V3A -> HALL_PWR_ON
- SW69 pad 6: +3V3A -> +3V3
- SW7 pad 1: +3V3A -> +3V3
- SW7 pad 5: +3V3A -> HALL_PWR_ON
- SW7 pad 6: +3V3A -> +3V3
- SW70 pad 1: +3V3A -> +3V3
- SW70 pad 5: +3V3A -> HALL_PWR_ON
- SW70 pad 6: +3V3A -> +3V3
- SW71 pad 1: +3V3A -> +3V3
- SW71 pad 5: +3V3A -> HALL_PWR_ON
- SW71 pad 6: +3V3A -> +3V3
- SW72 pad 1: +3V3A -> +3V3
- SW72 pad 5: +3V3A -> HALL_PWR_ON
- SW72 pad 6: +3V3A -> +3V3
- SW73 pad 1: +3V3A -> +3V3
- SW73 pad 5: +3V3A -> HALL_PWR_ON
- SW73 pad 6: +3V3A -> +3V3
- SW74 pad 1: +3V3A -> +3V3
- SW74 pad 5: +3V3A -> HALL_PWR_ON
- SW74 pad 6: +3V3A -> +3V3
- SW75 pad 1: +3V3A -> +3V3
- SW75 pad 5: +3V3A -> HALL_PWR_ON
- SW75 pad 6: +3V3A -> +3V3
- SW76 pad 1: +3V3A -> +3V3
- SW76 pad 5: +3V3A -> HALL_PWR_ON
- SW76 pad 6: +3V3A -> +3V3
- SW77 pad 1: +3V3A -> +3V3
- SW77 pad 5: +3V3A -> HALL_PWR_ON
- SW77 pad 6: +3V3A -> +3V3
- SW78 pad 1: +3V3A -> +3V3
- SW78 pad 5: +3V3A -> HALL_PWR_ON
- SW78 pad 6: +3V3A -> +3V3
- SW79 pad 1: +3V3A -> +3V3
- SW79 pad 5: +3V3A -> HALL_PWR_ON
- SW79 pad 6: +3V3A -> +3V3
- SW8 pad 1: +3V3A -> +3V3
- SW8 pad 5: +3V3A -> HALL_PWR_ON
- SW8 pad 6: +3V3A -> +3V3
- SW80 pad 1: +3V3A -> +3V3
- SW80 pad 5: +3V3A -> HALL_PWR_ON
- SW80 pad 6: +3V3A -> +3V3
- SW9 pad 1: +3V3A -> +3V3
- SW9 pad 5: +3V3A -> HALL_PWR_ON
- SW9 pad 6: +3V3A -> +3V3
- U1 pad 1: +5V -> Net-(U1-TS)
- U1 pad 2: unconnected-(U1-NC-Pad2) -> BAT+
- U1 pad 3: GND -> BAT+
- U1 pad 4: unconnected-(U1-NC-Pad4) -> GND
- U1 pad 5: unconnected-(U1-NC-Pad5) -> +5V
- U1 pad 6: +3V3 -> GND
- U1 pad 7: GND -> unconnected-(U1-~{PGOOD}-Pad7)
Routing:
- net HALL_PWR_ON: track 0.00 -> 2223.9 mm, vias 0 -> 49
- net +3V3: track 110.3 -> 213.3 mm, vias 22 -> 146
- net MUX_4: track 198.3 -> 112.9 mm, vias 5 -> 4
- net GND: track 441.2 -> 363.1 mm, vias 145 -> 161
- net SELECT1: track 575.6 -> 630.8 mm, vias 10 -> 8
- net SELECT0: track 572.2 -> 625.2 mm, vias 13 -> 8
- net WAKE_UP_FPRINT: track 0.00 -> 49.8 mm
- net +5V: track 33.6 -> 80.8 mm
- net RXD_FPRINT: track 0.00 -> 47.1 mm, vias 0 -> 2
- net TXD_FPRINT: track 0.00 -> 46.9 mm, vias 0 -> 2
- net SELECT3: track 557.5 -> 603.6 mm, vias 10 -> 12
- net MUX_2: track 262.4 -> 303.4 mm, vias 3 -> 2
- net SWDIO: track 35.9 -> 0.00 mm, vias 1 -> 0
- net MUX_3: track 177.5 -> 212.3 mm, vias 3 -> 4
- net SWCLK: track 34.6 -> 0.00 mm, vias 1 -> 0
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- added copper zone on F.Cu, net BAT+
- added copper zone on F.Cu, net Net-(U4-EN)
- removed copper zone on B.Cu, net +3V3A
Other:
- board size 317.8 x 142.5 mm -> 357.7 x 133.8 mm

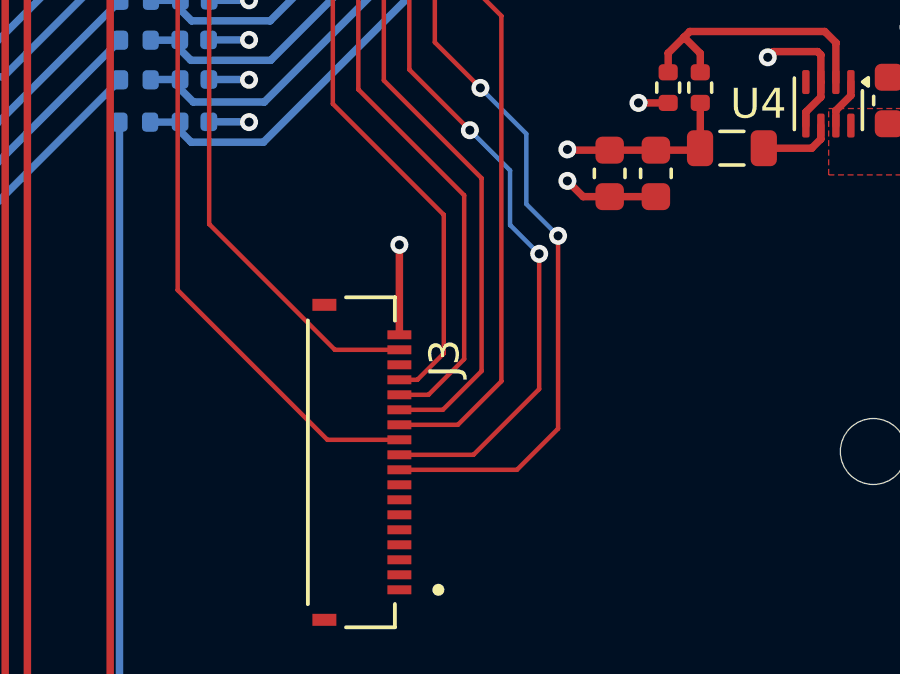
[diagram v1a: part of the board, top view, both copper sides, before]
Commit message: add forgotten display passive components
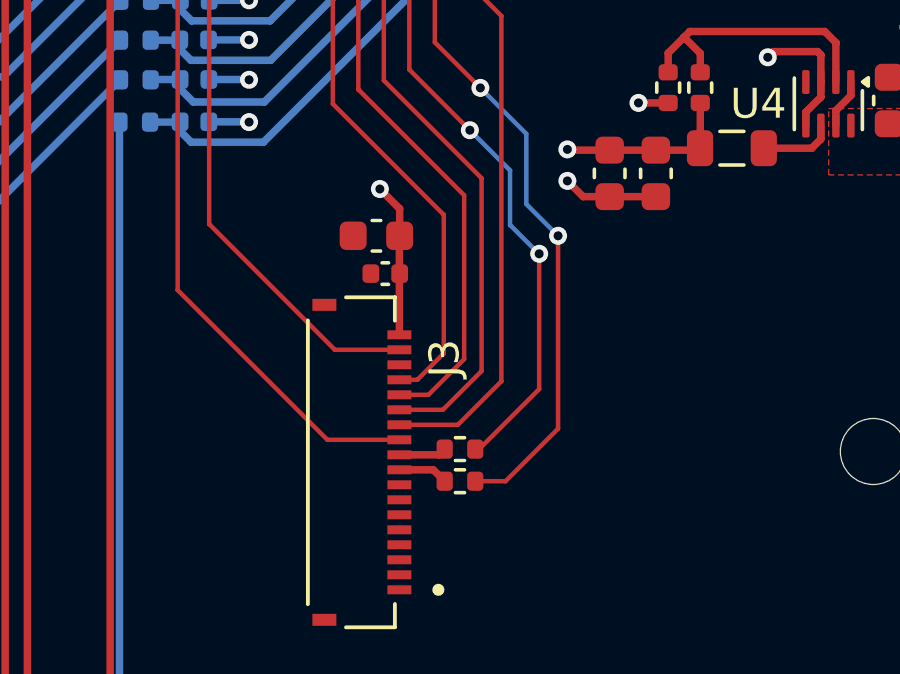
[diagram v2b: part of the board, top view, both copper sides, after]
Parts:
- added C86: 0.1uF, Capacitor_SMD:C_0402_1005Metric, F.Cu at (350.3, 58.7)
- added C87: 10uF, Capacitor_SMD:C_0603_1608Metric, F.Cu at (350.0, 57.5)
- added R11: 10K, Resistor_SMD:R_0402_1005Metric, F.Cu at (352.8, 65.7)
- added R19: 10K, Resistor_SMD:R_0402_1005Metric, F.Cu at (352.8, 64.6)
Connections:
- J3 pad 10: TCS -> Net-(J3-Pin_10)
- J3 pad 9: SDCS -> Net-(J3-Pin_9)
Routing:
- net TCS: track 24.9 -> 22.3 mm
- net SDCS: track 26.4 -> 24.1 mm
- net +3V3: track 213.3 -> 215.4 mm
- net Net-(J3-Pin_9): track 0.00 -> 1.67 mm
- net Net-(J3-Pin_10): track 0.00 -> 1.59 mm
